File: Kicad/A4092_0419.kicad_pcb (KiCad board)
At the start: 4 copper layers, 175.6 x 122.1 mm, 106 parts, among them CN1 Zorro3, J1 Conn_02x25_Odd_Even, J2 Conn_01x06_Pin, J3 TO-LED, J4 TO-MB, J5 5787170-5, J7 22112042, J8 TO-A3000-LED, J9 TO-A3000-MB, SW1 219-8MST, U1 SN74ABT16543DGGR, U10 NCR53c710 SCSI Host Controller, U11 DS21S07A, U12 DS21S07A, U13 SST39SF010/020/040, U2 SN74ABT16543DGGR, U3 SN74ABT16543DGGR, U4 SN74ABT16543DGGR, U5 74LVC07APW_118, U6 SN74ABT16245ADGGR, U7 AMS1117-3.3, U8 SN74F244DB, U9 XC95144XL-TQ144, Y1 Abracon ACO-50MHz

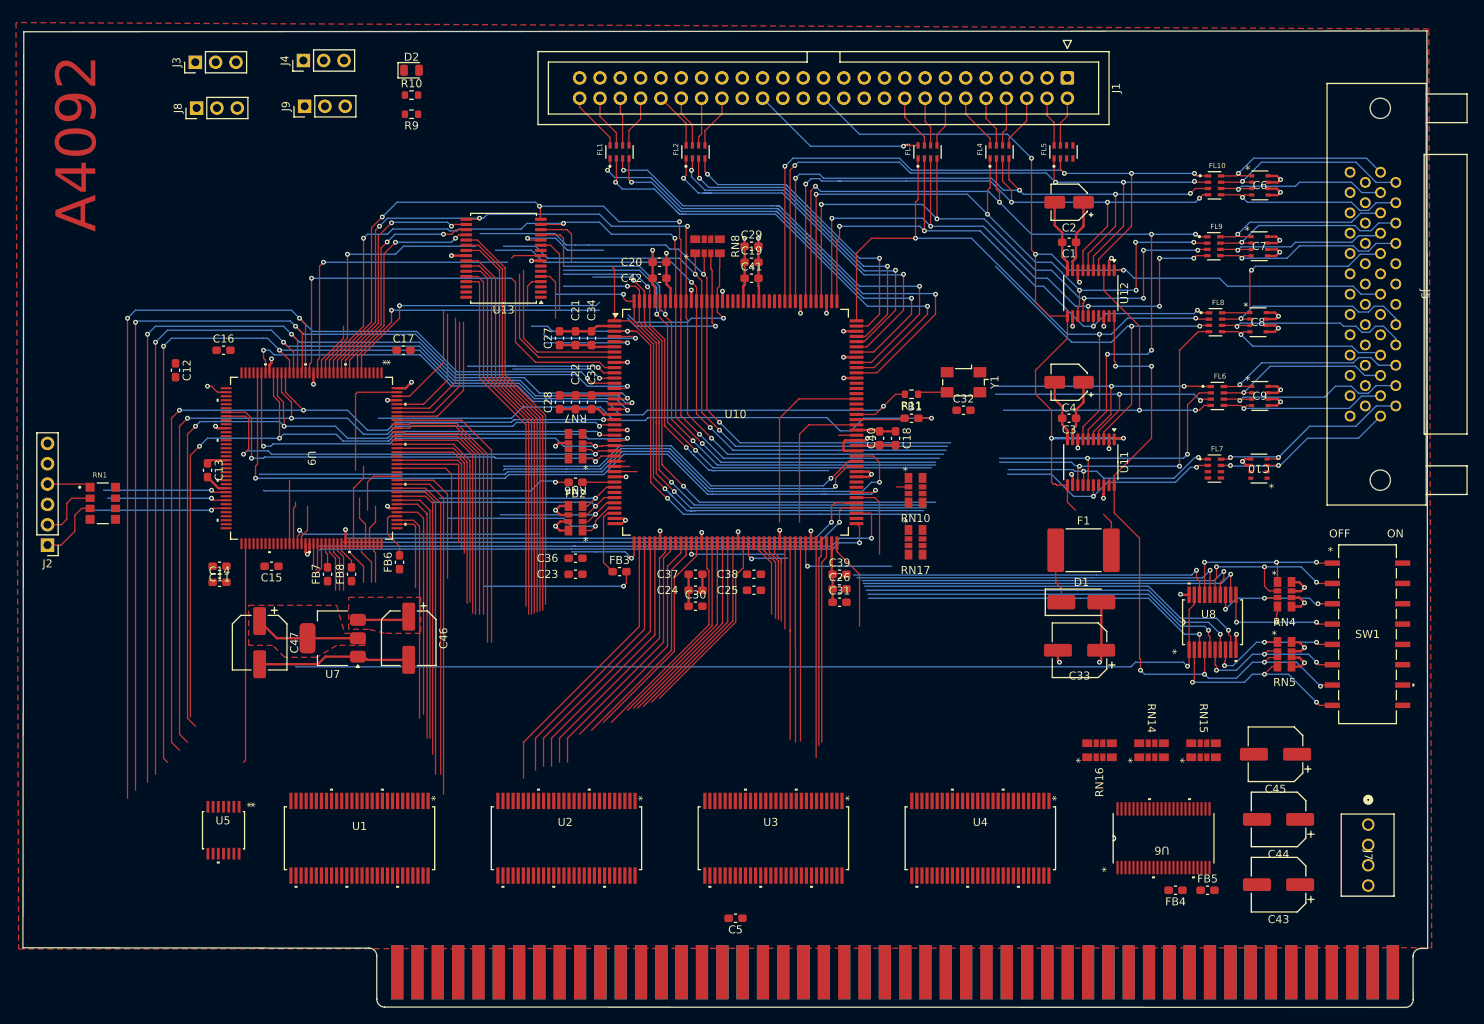
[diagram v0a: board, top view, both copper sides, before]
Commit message: CPLD Routing
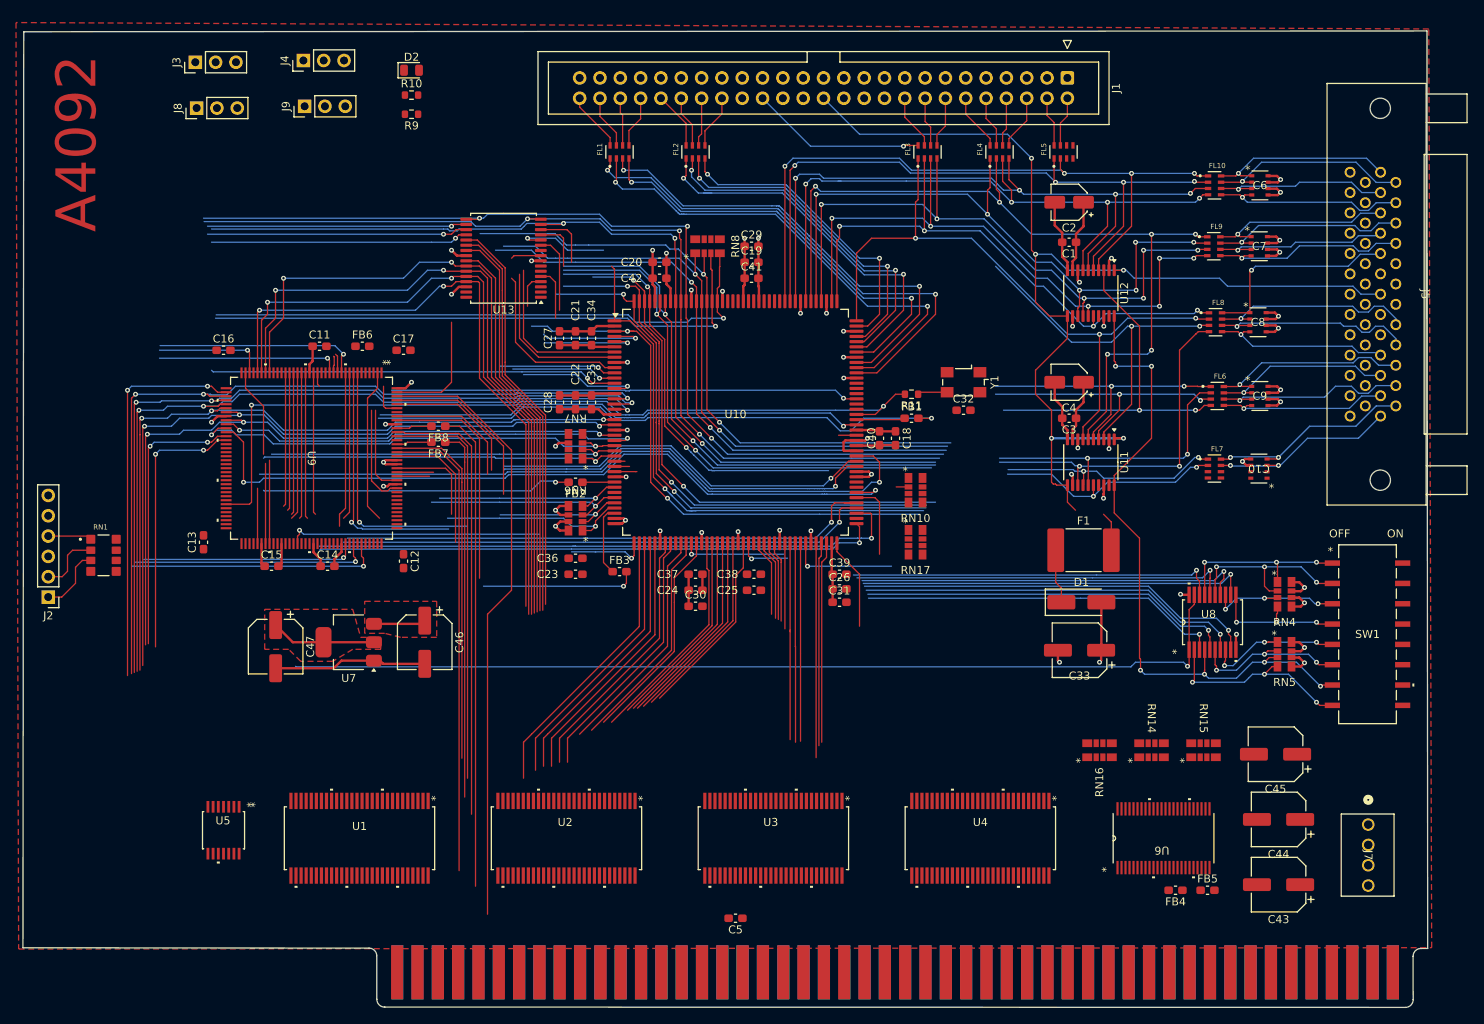
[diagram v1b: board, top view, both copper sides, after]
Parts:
- moved C12 37.2 mm to (96.5, 98.9)
- moved C11 30.2 mm to (86.0, 72.0), turned to 0 degrees
- moved FB6 27.4 mm to (91.4, 72.0), turned to 0 degrees
- moved FB7 21.5 mm to (100.9, 84.0), turned to 180 degrees
- moved FB8 21.4 mm to (100.9, 82.0), turned to 180 degrees
- moved C14 13.6 mm to (87.0, 99.5)
- moved C13 9.01 mm to (71.5, 96.5), turned to 90 degrees
- moved J2 6.50 mm to (52.1, 103.3)
- moved RN1 6.50 mm to (59.0, 98.1)
- moved C46 2.06 mm to (99.2, 109.0)
- moved C47 2.06 mm to (80.5, 109.5)
- moved U7 2.06 mm to (89.7, 109.0)
- turned C15 to 0 degrees
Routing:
- net A24: track 131.4 -> 33.6 mm, vias 3 -> 1
- net V3_3: track 16.8 -> 92.6 mm
- net ROM_CE: track 14.1 -> 78.6 mm, vias 0 -> 1
- net A23: track 132.2 -> 69.3 mm, vias 3 -> 1
- net NCR_INT: track 29.0 -> 90.6 mm, vias 0 -> 2
- net Z2D: track 0.00 -> 60.1 mm
- net A1: track 56.4 -> 104.8 mm
- net DBOE: track 0.00 -> 46.4 mm
- net A31: track 99.7 -> 53.4 mm, vias 3 -> 2
- net Z_7M: track 2.64 -> 48.5 mm, vias 1 -> 2
- net GND: track 156.2 -> 202.0 mm, vias 44 -> 40
- net Z_CFGOUT: track 43.6 -> 1.78 mm, vias 0 -> 1
- net Z_SENSEZ3: track 39.3 -> 0.00 mm
- net D3: track 141.0 -> 179.5 mm
- net D31: track 95.7 -> 132.8 mm, vias 0 -> 2
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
